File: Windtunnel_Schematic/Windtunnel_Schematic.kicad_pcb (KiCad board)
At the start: 2 copper layers, 91.4 x 71.1 mm, 14 parts, among them J3 Conn_01x09, J4 Screw_Terminal_01x06, J5 Screw_Terminal_01x06

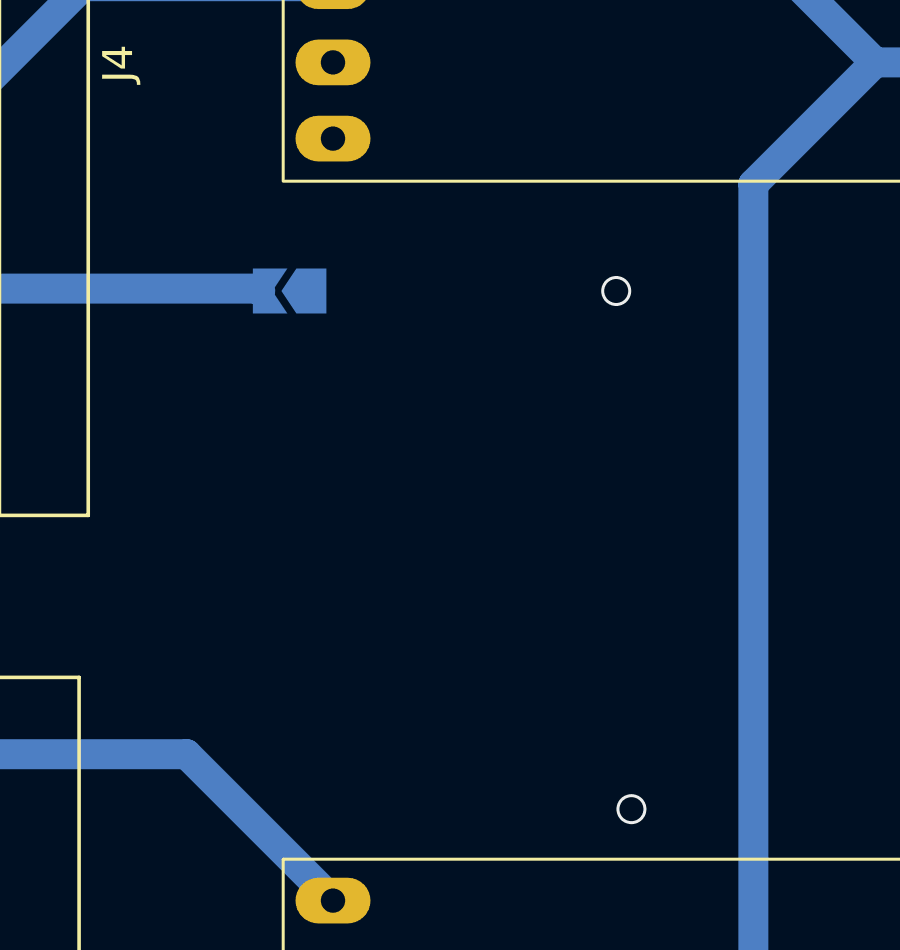
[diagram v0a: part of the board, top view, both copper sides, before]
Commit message: Add to docs, schematic and general calculation: ADD prototype data Change Schematic revision to 0.4.0 ADD requirements.txt for each general calculation virtual environment
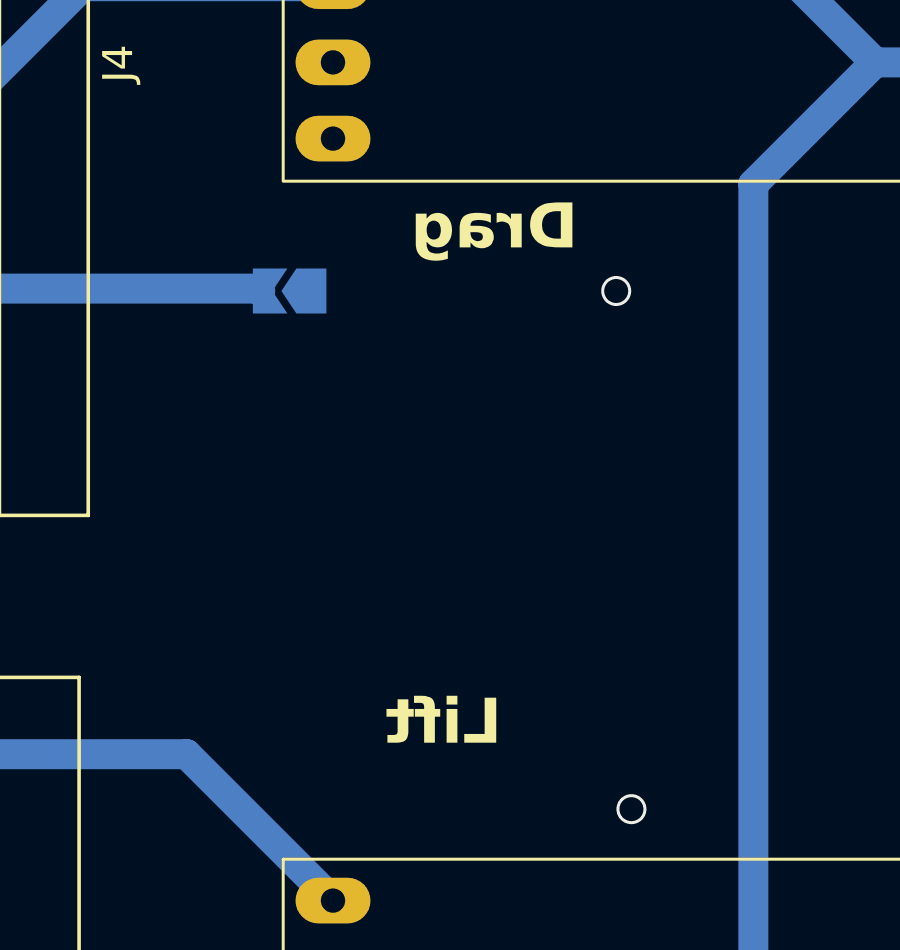
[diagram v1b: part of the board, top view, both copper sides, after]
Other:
- board text added: "Drag"
- board text added: "Lift"
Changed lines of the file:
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@@
 		(layer "Edge.Cuts")
+	)
+	(gr_text "Lift"
+		(at 77.47 124.46 0)
+		(layer "F.SilkS")
+		(effects
+			(font
+				(size 1.5 1.5)
+				(thickness 0.3)
+				(bold yes)
+			)
+			(justify left bottom mirror)
+		)
+	)
+	(gr_text "Drag"
+		(at 80.01 107.95 0)
+		(layer "F.SilkS")
+		(effects
+			(font
+				(size 1.5 1.5)
+				(thickness 0.3)
+				(bold yes)
+			)
+			(justify left bottom mirror)
+		)
 	)
 	(segment
